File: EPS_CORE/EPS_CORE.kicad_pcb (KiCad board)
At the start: 6 copper layers, 90 x 95.8 mm, 309 parts, among them IC1401 TPS259802ONRGER, IC1402 TPS259802ONRGER, IC1601 TPS259802ONRGER, IC1602 TPS259802ONRGER, IC301 TPS259802ONRGER, IC302 TPS259802ONRGER, IC601 TPS259802ONRGER, IC602 TPS259802ONRGER, IC801 TPS259802ONRGER, IC802 TPS259802ONRGER, J101 CAN, J102 BATT_PACK, J103 RS-485, J104 BATT_PACK, J106 OUT, J902 JTAG, J903 JTAG, Q1001 NVTFWS4D9N04XMTAG, Q1002 NVTFWS4D9N04XMTAG, Q1003 BSS138L, Q201 NVTFWS4D9N04XMTAG, Q202 NVTFWS4D9N04XMTAG, SW101 Deploy, U1001 TPS62933, U1002 LM74700, U1003 TPS62933, U1004 LM74700, U101 LP38690SDX-3.3/NOPB, U1101 THVD1424, U1701 TMCS1101A2UQDT, U1801 TMCS1101A2UQDT, U201 LM74700, U202 LM74700, U401 TMCS1101A2UQDT, U901 LP38690SDX-3.3/NOPB, U902 MSP430FR5969IRGZR, U903 ADG1607xCP, U904 MSP430FR5969IRGZR, U905 TCAN4551RGYRQ1, U906 ADG1607xCP, Y901 Crystal, Y902 Crystal

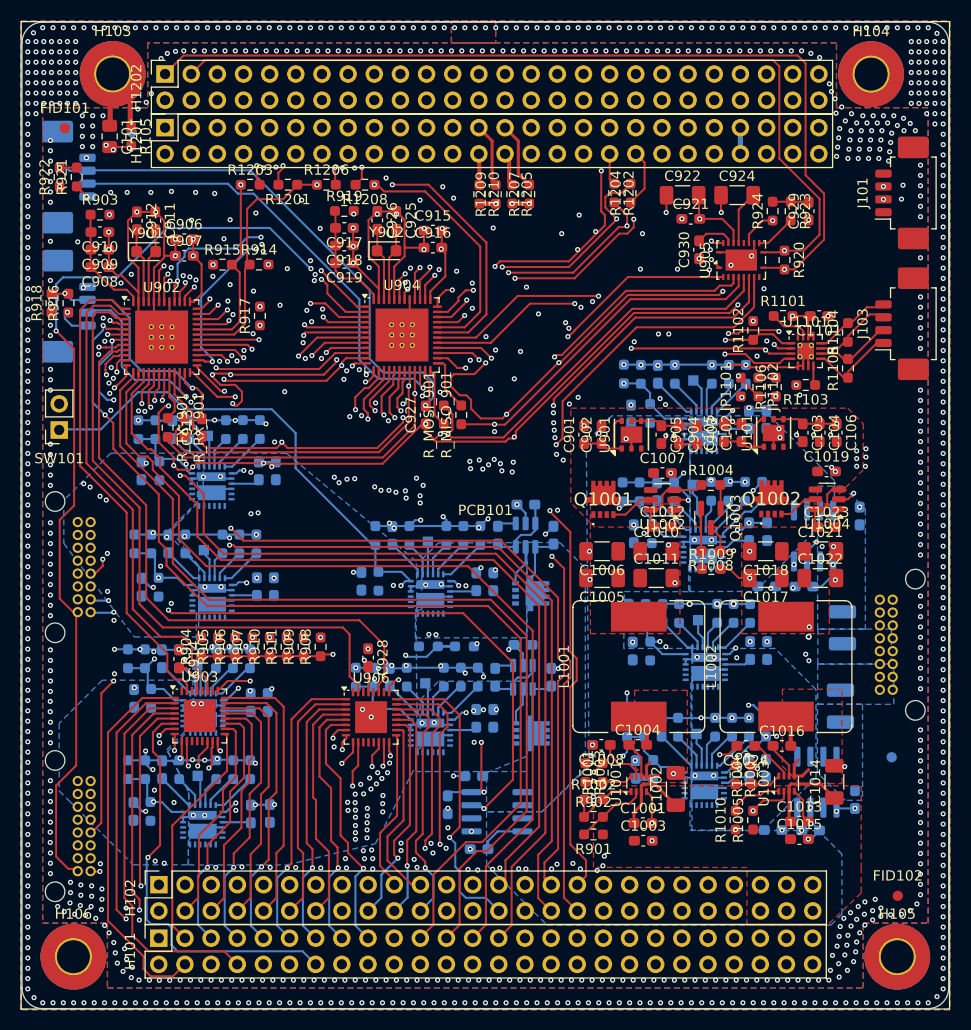
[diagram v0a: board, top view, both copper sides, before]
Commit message: pcb progres for all components
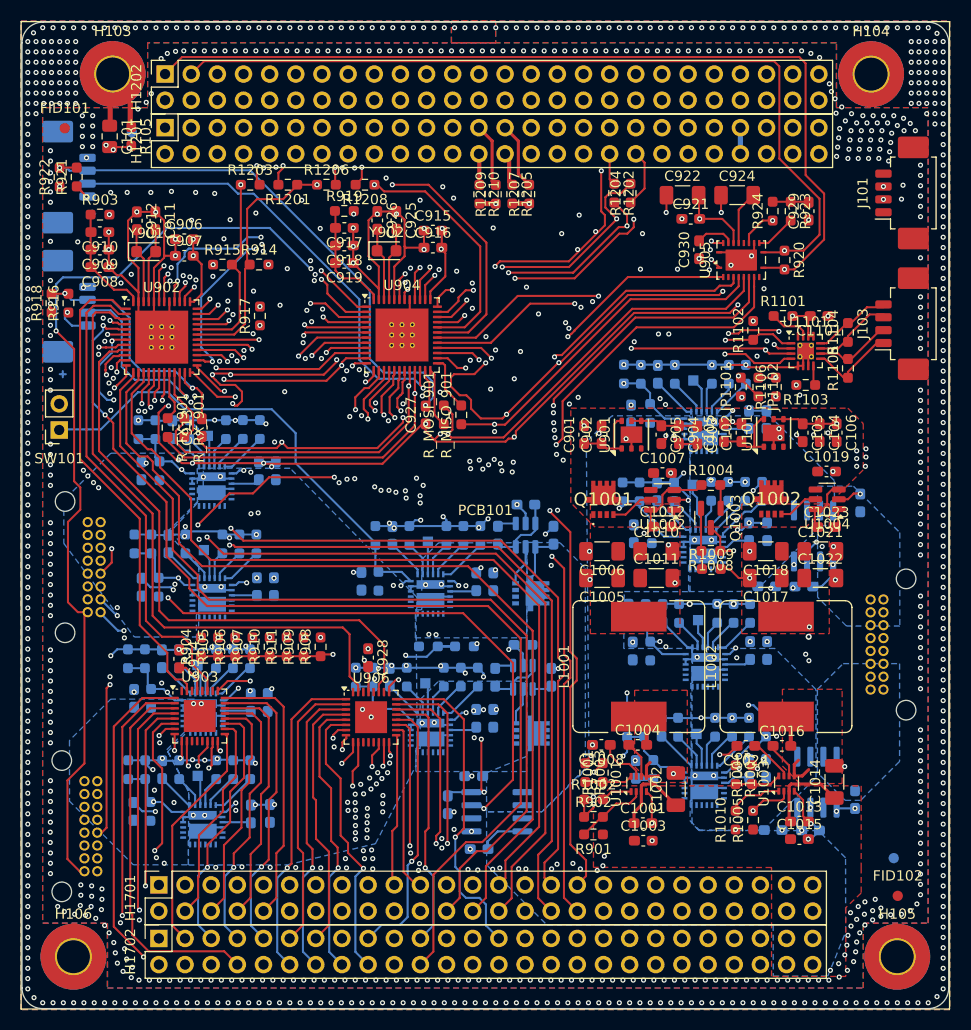
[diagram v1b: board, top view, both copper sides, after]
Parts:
- removed H101, H102: PC104, Connector_PinSocket_2.54mm:PinSocket_2x26_P2.54mm_Vertical
- removed J106: OUT, Outlines:G125-MH11605L1P
- removed R101, R102: 0, Resistor_SMD:R_1210_3225Metric_Pad1.30x2.65mm_HandSolder
- added H1701: PC104, Connector_PinSocket_2.54mm:PinSocket_2x26_P2.54mm_Vertical, F.Cu at (53.9, 127.2)
- added H1702: PC104, Connector_PinSocket_2.54mm:PinSocket_2x26_P2.54mm_Vertical, F.Cu at (53.9, 132.4)
- added J107: BUS_OUT, Outlines:G125-MH11605L1P, B.Cu at (123.0, 108.2)
- moved FID104 9.80 mm to (125.2, 124.6)
- moved C1803 1.27 mm to (122.0, 90.1)
- moved J104 0.97 mm to (48.2, 92.0)
- moved J102 0.65 mm to (47.9, 117.1)
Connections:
- C1703 pad 1: /AMEAS_9/VOUT -> /Channel_9
- C1803 pad 1: /AMEAS_10/VOUT -> /Channel_10
- U1701 pad 3: /AMEAS_9/VOUT -> /Channel_9
- U1701 pad 4: /AMEAS_9/VOUT -> /Channel_9
- U1801 pad 3: /AMEAS_10/VOUT -> /Channel_10
- U1801 pad 4: /AMEAS_10/VOUT -> /Channel_10
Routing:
- net /SOL_STAT_1: track 70.4 -> 82.4 mm
- net GND: track 740.2 -> 752.0 mm, vias 776 -> 758
- net /SW_BATT_12: track 50.8 -> 60.0 mm, vias 3 -> 4
- net /SOL_EN_6: track 71.6 -> 80.0 mm
- net /Ch_AL_6: track 84.9 -> 77.2 mm
- net /Ch_V_1: track 40.7 -> 33.6 mm
- net /SOL_EN_5: track 66.7 -> 72.4 mm
- net /Ch_AL_5: track 73.7 -> 68.5 mm
- net /Ch_V_2: track 39.1 -> 34.0 mm
- net /VMEAS_SOL_2: track 21.1 -> 26.0 mm
- net /VMEAS_SOL_1: track 21.2 -> 25.9 mm
- net /BUS: track 98.2 -> 102.5 mm
- net SCL: track 133.0 -> 136.4 mm
- net +3V3: track 152.4 -> 149.3 mm, vias 8 -> 7
- net /AMEAS_SOL_5: track 24.5 -> 27.2 mm
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- removed copper zone on B.Cu, net /AMEAS_10/VOUT
- removed copper zone on B.Cu, net /AMEAS_9/VOUT
